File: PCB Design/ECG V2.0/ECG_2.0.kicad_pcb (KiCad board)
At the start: 4 copper layers, 42.2 x 53.8 mm, 50 parts, among them J1 01x05_Female, J2 JST_01x04_Male, U1 Li-Po, U10 ESP32-C3-MINI-1-N4, U11 FS8205A, U12 DW01, U2 TP4056-C21417, U3 USBLC6-2SC6, U4 Battery_Switch, U5 5V_switch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

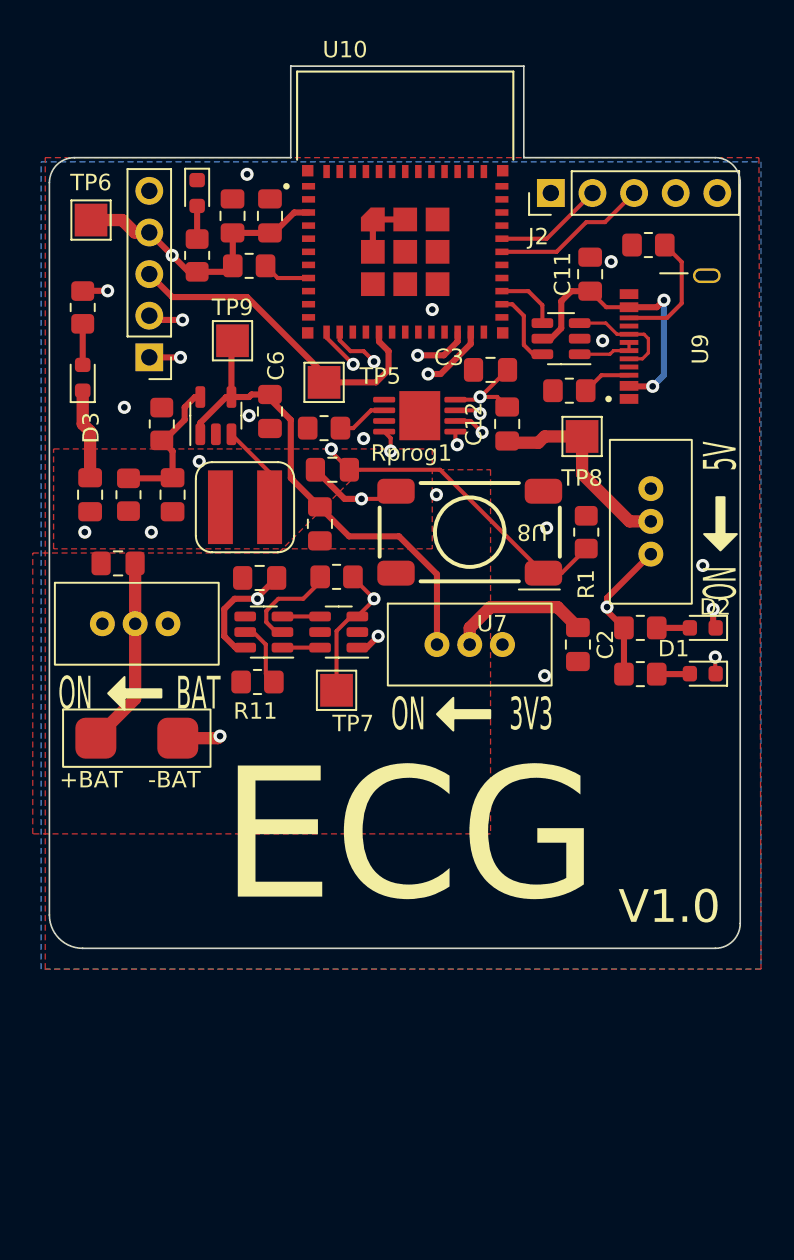
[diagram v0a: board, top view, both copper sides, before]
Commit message: Gerber files and Larger pcb due to manufacturing limits
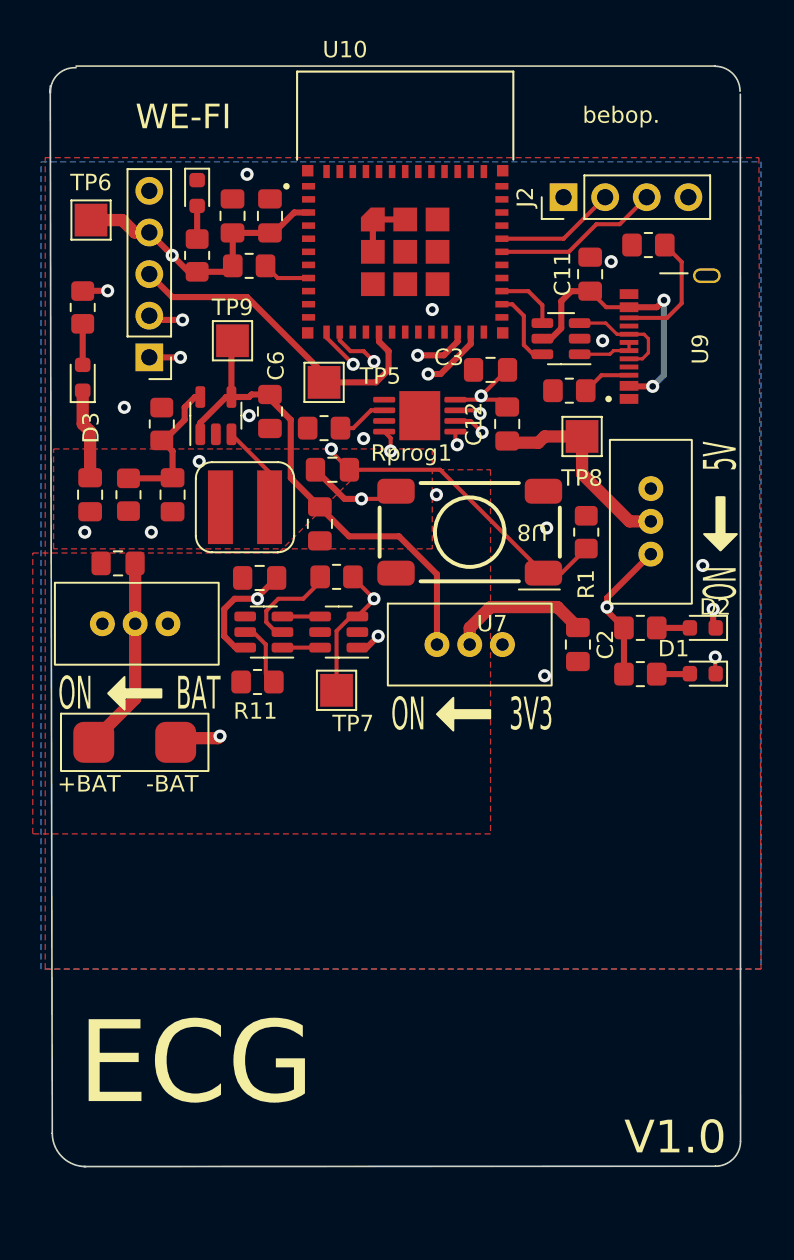
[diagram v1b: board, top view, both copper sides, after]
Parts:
- C4: value 0.1uF -> 100nF
- J2: footprint Connector_PinHeader_2.54mm:PinHeader_1x05_P2.54mm_Vertical -> Connector_PinHeader_2.54mm:PinHeader_1x04_P2.54mm_Vertical
- moved J2 0.81 mm to (245.2, 77.1)
- moved U1 0.28 mm to (218.8, 110.4)
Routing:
- net /TX: track 6.69 -> 7.35 mm
- net /RX: track 9.56 -> 10.2 mm
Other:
- board size 42.2 x 53.8 mm -> 42.1 x 67.2 mm
- board text added: "WE-FI"
- board text added: "bebop."

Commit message: Final pcb
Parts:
- renumbered TP6 to 3V3, TP9 to 4V, TP8 to 5V, TP7 to GND, TP5 to OUT
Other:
- board size 42.1 x 67.2 mm -> 42.3 x 69.7 mm
- board text added: "LI-PO"
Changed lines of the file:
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@@
       (drillshape 0)
       (scaleselection 1)
-      (outputdirectory "JLPCB/gerbers/")
+      (outputdirectory "JLPCB/")
     )
   )
@@
     (property "Vendor" "C115423")
     (attr smd)
-    (fp_text reference "R11" (at 0.127 -1.778) (layer "F.SilkS")
+    (fp_text reference "R11" (at 0.127 -1.778) (layer "F.SilkS") hide
       (effects (font (size 1 1) (thickness 0.15)))
     )
@@
     (property "Vendor" "C38141")
     (attr smd)
-    (fp_text reference "C12" (at 0 2.032 90) (layer "F.SilkS")
+    (fp_text reference "C12" (at 0 2.032 90) (layer "F.SilkS") hide
       (effects (font (size 1 1) (thickness 0.15)))
     )
@@
     (property "Vendor" "C2838502")
     (attr smd)
-    (fp_text reference "U10" (at -3.675 -9.635) (layer "F.SilkS")
+    (fp_text reference "U10" (at -3.675 -9.635) (layer "F.SilkS") hide
       (effects (font (size 1 1) (thickness 0.15)))
     )
@@
     (property "Vendor" "C17414")
     (attr smd)
-    (fp_text reference "R1" (at -3.175 0 90) (layer "F.SilkS")
+    (fp_text reference "R1" (at -3.175 0 90) (layer "F.SilkS") hide
       (effects (font (size 1 1) (thickness 0.15)))
     )
@@
     (property "Vendor" "C273519")
     (attr smd)
-    (fp_text reference "U8" (at -3.81 0 180 unlocked) (layer "F.SilkS")
+    (fp_text reference "U8" (at -3.81 0 180 unlocked) (layer "F.SilkS") hide
       (effects (font (size 1 1) (thickness 0.15)))
     )
@@
     (property "Sheetname" "")
     (attr exclude_from_pos_files)
-    (fp_text reference "TP8" (at 0 2.54) (layer "F.SilkS")
+    (fp_text reference "5V" (at 0 2.54) (layer "F.SilkS")
       (effects (font (size 1 1) (thickness 0.15)))
     )
@@
     (property "Sheetname" "")
     (attr exclude_from_pos_files)
-    (fp_text reference "TP7" (at 1.016 2.032) (layer "F.SilkS")
+    (fp_text reference "GND" (at -0.254 2.54) (layer "F.SilkS")
       (effects (font (size 1 1) (thickness 0.15)))
     )
@@
     (property "Vendor" "C5116483")
     (attr through_hole)
-    (fp_text reference "J2" (at 0 -2.33 90) (layer "F.SilkS")
+    (fp_text reference "J2" (at 0 -2.33 90) (layer "F.SilkS") hide
       (effects (font (size 1 1) (thickness 0.15)))
     )
@@
     (property "Vendor" "C412634")
     (attr smd)
-    (fp_text reference "C6" (at -2.794 -0.3685 -90) (layer "F.SilkS")
+    (fp_text reference "C6" (at -2.794 -0.3685 -90) (layer "F.SilkS") hide
       (effects (font (size 1 1) (thickness 0.15)))
     )
@@
     (property "Vendor" "C709357")
     (attr smd)
-    (fp_text reference "U9" (at -0.155 -0.3925 90) (layer "F.SilkS")
+    (fp_text reference "U9" (at -0.155 -0.3925 90) (layer "F.SilkS") hide
       (effects (font (size 1 1) (thickness 0.15)))
     )
@@
     (property "Vendor" "C84263")
     (attr smd)
-    (fp_text reference "D1" (at 1.778 -1.27) (layer "F.SilkS")
+    (fp_text reference "D1" (at 1.778 -1.27) (layer "F.SilkS") hide
       (effects (font (size 1 1) (thickness 0.125)))
     )
@@
     (property "Vendor" "C17388")
     (attr smd)
-    (fp_text reference "Rprog1" (at -5.334 -1.524 180) (layer "F.SilkS")
+    (fp_text reference "Rprog1" (at -5.334 -1.524 180) (layer "F.SilkS") hide
       (effects (font (size 1 1) (thickness 0.15)))
     )
@@
     (property "Vendor" "C264469")
     (attr smd)
-    (fp_text reference "D3" (at -3.048 0.508 90) (layer "F.SilkS")
+    (fp_text reference "D3" (at -3.048 0.508 90) (layer "F.SilkS") hide
       (effects (font (size 1 1) (thickness 0.15)))
     )
@@
     (property "Vendor" "C1713")
     (attr smd)
-    (fp_text reference "C2" (at 0 -1.68 -270) (layer "F.SilkS")
+    (fp_text reference "C2" (at 0 -1.68 -270) (layer "F.SilkS") hide
       (effects (font (size 1 1) (thickness 0.15)))
     )
@@
     (property "Sheetname" "")
     (attr exclude_from_pos_files)
-    (fp_text reference "TP5" (at 3.429 -0.381) (layer "F.SilkS")
+    (fp_text reference "OUT" (at 3.048 0) (layer "F.SilkS")
       (effects (font (size 1 1) (thickness 0.15)))
     )
@@
     (property "Sheetname" "")
     (attr exclude_from_pos_files)
-    (fp_text reference "TP9" (at 0 -2.032) (layer "F.SilkS")
+    (fp_text reference "4V" (at 0 -2.032) (layer "F.SilkS")
       (effects (font (size 1 1) (thickness 0.15)))
     )
@@
     (property "Sheetname" "")
     (attr exclude_from_pos_files)
-    (fp_text reference "TP6" (at 0 -2.286) (layer "F.SilkS")
+    (fp_text reference "3V3" (at 0 -2.286) (layer "F.SilkS")
       (effects (font (size 1 1) (thickness 0.15)))
     )
@@
     (property "Vendor" "C1713")
     (attr smd)
-    (fp_text reference "C3" (at 2.54 0.762 180) (layer "F.SilkS")
+    (fp_text reference "C3" (at 2.54 0.762 180) (layer "F.SilkS") hide
       (effects (font (size 1 1) (thickness 0.15)))
     )
@@
     (property "Vendor" "C1713")
     (attr smd)
-    (fp_text reference "C11" (at 0 -1.68 90) (layer "F.SilkS")
+    (fp_text reference "C11" (at 0 -1.68 90) (layer "F.SilkS") hide
       (effects (font (size 1 1) (thickness 0.15)))
     )
@@
     )
   )
-  (gr_line (start 256.039349 70.804305) (end 256.05018 134.710705) (layer "Edge.Cuts") (width 0.1))
-  (gr_line (start 254.52618 136.234705) (end 215.983421 136.256495) (layer "Edge.Cuts") (width 0.1))
-  (gr_arc (start 216.07419 136.256495) (mid 214.637349 135.661336) (end 214.04219 134.224495) (layer "Edge.Cuts") (width 0.1))
-  (gr_arc (start 256.05018 134.710705) (mid 255.603811 135.788336) (end 254.52618 136.234705) (layer "Edge.Cuts") (width 0.1))
-  (gr_arc (start 213.929631 70.724431) (mid 214.381807 69.594402) (end 215.4936 69.1896) (layer "Edge.Cuts") (width 0.1))
-  (gr_line (start 214.04219 134.224495) (end 213.9188 70.3072) (layer "Edge.Cuts") (width 0.1))
-  (gr_line (start 215.4936 69.088) (end 254.508 69.088) (layer "Edge.Cuts") (width 0.1))
-  (gr_arc (start 254.497169 69.098831) (mid 255.5748 69.5452) (end 256.021169 70.622831) (layer "Edge.Cuts") (width 0.1))
-  (gr_text "bebop." (at 248.7676 72.0852) (layer "F.SilkS")
+  (gr_rect (start 215.392 114.3) (end 255.016 138.176) (layer "F.SilkS") (width 0.15) (fill none))
+  (gr_line (start 254.508 138.684) (end 215.9 138.684) (layer "Edge.Cuts") (width 0.1))
+  (gr_arc (start 215.9 138.684) (mid 214.463159 138.088841) (end 213.868 136.652) (layer "Edge.Cuts") (width 0.1))
+  (gr_arc (start 254.508 69.031721) (mid 255.629418 69.49858) (end 256.088239 70.623311) (layer "Edge.Cuts") (width 0.1))
+  (gr_arc (start 213.811721 70.612) (mid 214.274574 69.494574) (end 215.392 69.031721) (layer "Edge.Cuts") (width 0.1))
+  (gr_arc (start 256.032 137.16) (mid 255.585631 138.237631) (end 254.508 138.684) (layer "Edge.Cuts") (width 0.1))
+  (gr_line (start 213.868 136.652) (end 213.811721 70.612) (layer "Edge.Cuts") (width 0.1))
+  (gr_line (start 256.088239 70.623311) (end 256.032 137.16) (layer "Edge.Cuts") (width 0.1))
+  (gr_line (start 215.392 69.031721) (end 254.508 69.031721) (layer "Edge.Cuts") (width 0.1))
+  (gr_text "bebop." (at 252.476 70.612) (layer "F.SilkS")
     (effects (font (size 1 1) (thickness 0.15)))
   )
-  (gr_text "WE-FI" (at 222.0468 72.1868) (layer "F.SilkS")
+  (gr_text "WE-FI" (at 220.472 72.1868) (layer "F.SilkS")
     (effects (font (size 1.5 1.5) (thickness 0.3)))
   )
-  (gr_text "V1.0" (at 252.0696 134.4676) (layer "F.SilkS")
+  (gr_text "LI-PO\n" (at 236.22 123.952) (layer "F.SilkS")
+    (effects (font (size 3 3) (thickness 0.4)))
+  )
+  (gr_text "V1.0" (at 251.46 136.652) (layer "F.SilkS")
     (effects (font (size 2 2) (thickness 0.4)))
   )
-  (gr_text "ECG" (at 222.8088 129.9464) (layer "F.SilkS")
+  (gr_text "ECG" (at 223.012 134.62) (layer "F.SilkS")
     (effects (font (size 5 5) (thickness 1.25)))
   )
@@
     (polygon
       (pts
-        (xy 257.302 124.206)
-        (xy 213.614 124.206)
+        (xy 257.302 116.078)
+        (xy 213.614 116.078)
         (xy 213.614 74.676)
         (xy 257.175 74.676)
@@
     (polygon
       (pts
-        (xy 258.572 124.1044)
-        (xy 212.09 124.1044)
+        (xy 258.572 115.9764)
+        (xy 212.09 115.9764)
         (xy 212.09 74.93)
         (xy 258.572 74.93)
@@
     (polygon
       (pts
-        (xy 259.588 124.0536)
-        (xy 211.328 124.0536)
+        (xy 259.588 115.9256)
+        (xy 211.328 115.9256)
         (xy 211.328 74.676)
         (xy 259.588 74.676)
@@
     (polygon
       (pts
-        (xy 257.302 124.206)
-        (xy 213.36 124.206)
+        (xy 257.302 116.078)
+        (xy 213.36 116.078)
         (xy 213.36 74.93)
         (xy 257.302 74.93)
